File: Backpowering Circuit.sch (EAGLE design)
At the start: 4 parts, among them IC1 DMMT5401, Q1 DMP2305U-7

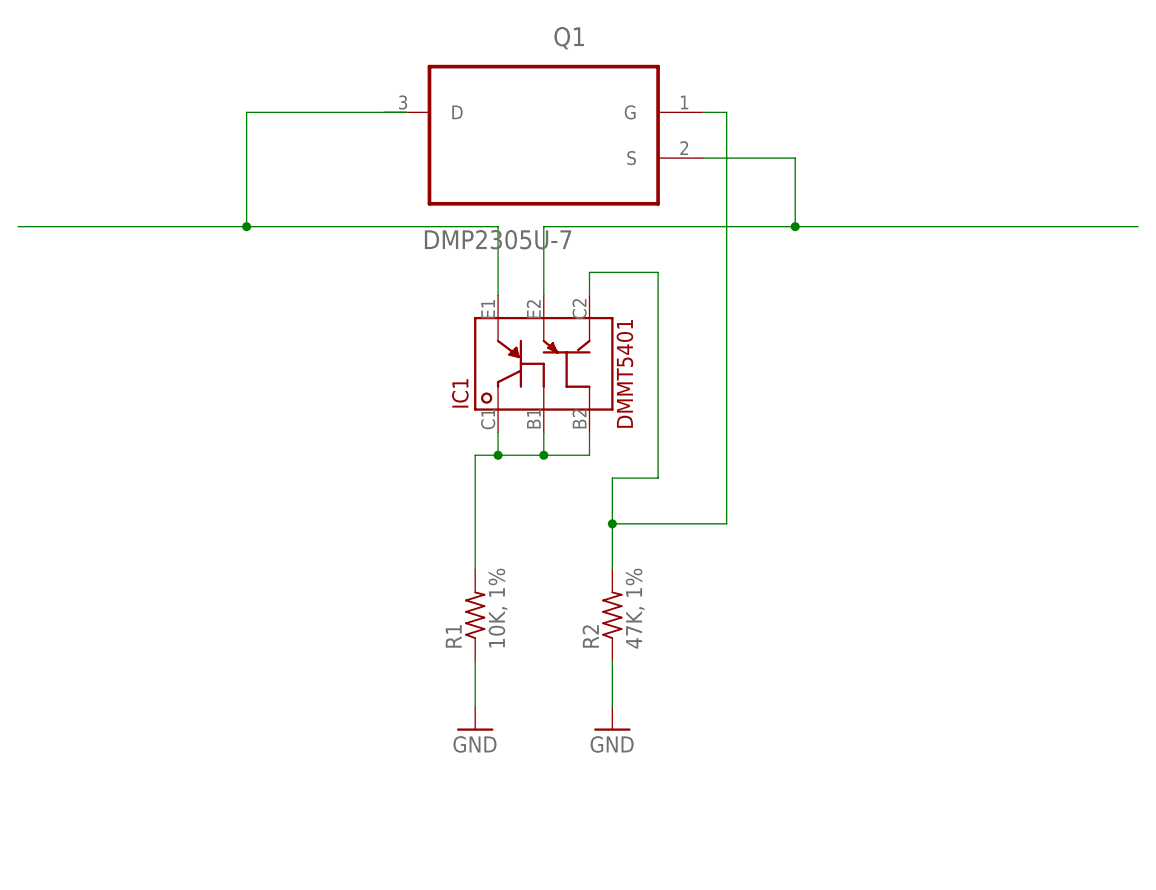
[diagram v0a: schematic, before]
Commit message: Convertd Backpowering Circuit schematic into a pluggable board.
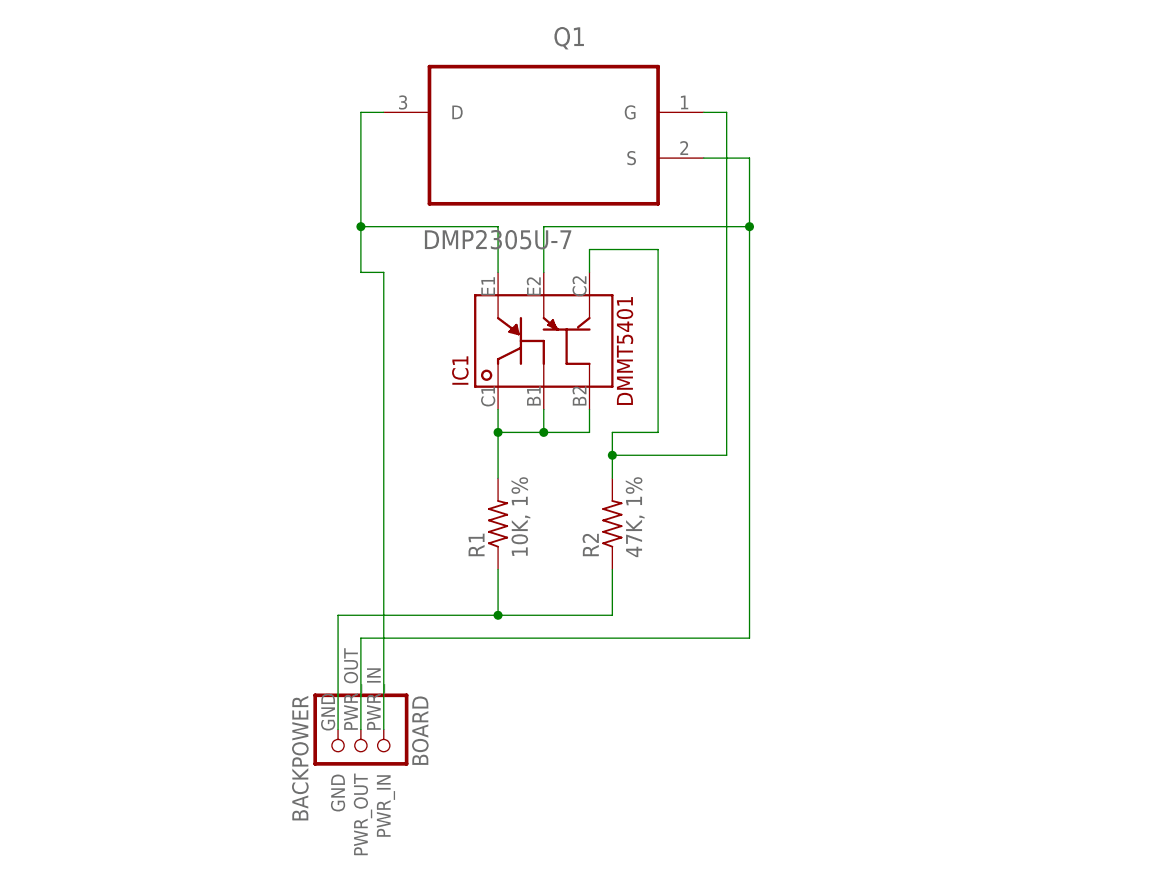
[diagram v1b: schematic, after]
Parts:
- added BOARD: BACKPOWER, connectors:BACKPOWER
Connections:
- removed net GND: R1.1, R2.1
- new net N$1: BOARD.GND, R1.1, R2.1
- net IN: now also BOARD.PWR_IN, Q1.D
- net OUT: now also BOARD.PWR_OUT
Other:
- moved on the sheet: IC1, R1, R2
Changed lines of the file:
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@@
 <part name="R1" library="adafruit" deviceset="R-US_" device="R1005" value="10K, 1%"/>
 <part name="R2" library="adafruit" deviceset="R-US_" device="R1005" value="47K, 1%"/>
-<part name="GND1" library="supply1" deviceset="GND" device=""/>
-<part name="GND2" library="supply1" deviceset="GND" device=""/>
+<part name="BOARD" library="connectors" deviceset="BACKPOWER" device=""/>
 </parts>
 <sheets>
@@
 <instances>
 <instance part="Q1" gate="A" x="27.94" y="71.12" rot="MR0"/>
-<instance part="IC1" gate="G$1" x="27.94" y="43.18"/>
-<instance part="R1" gate="G$1" x="20.32" y="15.24" rot="R90"/>
-<instance part="R2" gate="G$1" x="35.56" y="15.24" rot="R90"/>
-<instance part="GND1" gate="1" x="20.32" y="2.54"/>
-<instance part="GND2" gate="1" x="35.56" y="2.54"/>
+<instance part="IC1" gate="G$1" x="27.94" y="45.72"/>
+<instance part="R1" gate="G$1" x="22.86" y="25.4" rot="R90"/>
+<instance part="R2" gate="G$1" x="35.56" y="25.4" rot="R90"/>
+<instance part="BOARD" gate="G$1" x="7.62" y="0" rot="R270"/>
 </instances>
 <busses>
@@
 <net name="IN" class="0">
 <segment>
-<wire x1="-5.08" y1="58.42" x2="-30.48" y2="58.42" width="0.1524" layer="91"/>
-<wire x1="-5.08" y1="58.42" x2="-5.08" y2="71.12" width="0.1524" layer="91"/>
-<wire x1="-5.08" y1="71.12" x2="12.7" y2="71.12" width="0.1524" layer="91"/>
+<wire x1="7.62" y1="58.42" x2="7.62" y2="53.34" width="0.1524" layer="91"/>
+<wire x1="7.62" y1="58.42" x2="7.62" y2="71.12" width="0.1524" layer="91"/>
 <pinref part="IC1" gate="G$1" pin="E1"/>
-<wire x1="22.86" y1="50.8" x2="22.86" y2="58.42" width="0.1524" layer="91"/>
-<wire x1="22.86" y1="58.42" x2="-5.08" y2="58.42" width="0.1524" layer="91"/>
-<junction x="-5.08" y="58.42"/>
-</segment>
-</net>
-<net name="GND" class="0">
-<segment>
-<pinref part="GND1" gate="1" pin="GND"/>
-<pinref part="R1" gate="G$1" pin="1"/>
-<wire x1="20.32" y1="5.08" x2="20.32" y2="10.16" width="0.1524" layer="91"/>
-</segment>
-<segment>
-<pinref part="GND2" gate="1" pin="GND"/>
-<pinref part="R2" gate="G$1" pin="1"/>
-<wire x1="35.56" y1="5.08" x2="35.56" y2="10.16" width="0.1524" layer="91"/>
+<wire x1="22.86" y1="53.34" x2="22.86" y2="58.42" width="0.1524" layer="91"/>
+<wire x1="22.86" y1="58.42" x2="7.62" y2="58.42" width="0.1524" layer="91"/>
+<junction x="7.62" y="58.42"/>
+<pinref part="BOARD" gate="G$1" pin="PWR_IN"/>
+<wire x1="7.62" y1="53.34" x2="10.16" y2="53.34" width="0.1524" layer="91"/>
+<wire x1="10.16" y1="53.34" x2="10.16" y2="2.54" width="0.1524" layer="91"/>
+<pinref part="Q1" gate="A" pin="D"/>
+<wire x1="7.62" y1="71.12" x2="10.16" y2="71.12" width="0.1524" layer="91"/>
 </segment>
 </net>
 <net name="OUT" class="0">
 <segment>
-<wire x1="55.88" y1="58.42" x2="93.98" y2="58.42" width="0.1524" layer="91"/>
+<wire x1="50.8" y1="58.42" x2="50.8" y2="12.7" width="0.1524" layer="91"/>
 <pinref part="Q1" gate="A" pin="S"/>
-<wire x1="55.88" y1="58.42" x2="55.88" y2="66.04" width="0.1524" layer="91"/>
-<wire x1="55.88" y1="66.04" x2="45.72" y2="66.04" width="0.1524" layer="91"/>
+<wire x1="50.8" y1="58.42" x2="50.8" y2="66.04" width="0.1524" layer="91"/>
+<wire x1="50.8" y1="66.04" x2="45.72" y2="66.04" width="0.1524" layer="91"/>
 <pinref part="IC1" gate="G$1" pin="E2"/>
-<wire x1="27.94" y1="50.8" x2="27.94" y2="58.42" width="0.1524" layer="91"/>
-<wire x1="27.94" y1="58.42" x2="55.88" y2="58.42" width="0.1524" layer="91"/>
-<junction x="55.88" y="58.42"/>
+<wire x1="27.94" y1="53.34" x2="27.94" y2="58.42" width="0.1524" layer="91"/>
+<wire x1="27.94" y1="58.42" x2="50.8" y2="58.42" width="0.1524" layer="91"/>
+<junction x="50.8" y="58.42"/>
+<wire x1="50.8" y1="12.7" x2="7.62" y2="12.7" width="0.1524" layer="91"/>
+<pinref part="BOARD" gate="G$1" pin="PWR_OUT"/>
+<wire x1="7.62" y1="12.7" x2="7.62" y2="2.54" width="0.1524" layer="91"/>
 </segment>
 </net>
@@
 <segment>
 <pinref part="IC1" gate="G$1" pin="C1"/>
-<wire x1="22.86" y1="35.56" x2="22.86" y2="33.02" width="0.1524" layer="91"/>
-<wire x1="22.86" y1="33.02" x2="20.32" y2="33.02" width="0.1524" layer="91"/>
+<wire x1="22.86" y1="38.1" x2="22.86" y2="35.56" width="0.1524" layer="91"/>
 <pinref part="R1" gate="G$1" pin="2"/>
-<wire x1="20.32" y1="33.02" x2="20.32" y2="20.32" width="0.1524" layer="91"/>
+<wire x1="22.86" y1="35.56" x2="22.86" y2="30.48" width="0.1524" layer="91"/>
 <pinref part="IC1" gate="G$1" pin="B1"/>
-<wire x1="27.94" y1="35.56" x2="27.94" y2="33.02" width="0.1524" layer="91"/>
-<wire x1="27.94" y1="33.02" x2="22.86" y2="33.02" width="0.1524" layer="91"/>
-<junction x="22.86" y="33.02"/>
+<wire x1="27.94" y1="38.1" x2="27.94" y2="35.56" width="0.1524" layer="91"/>
+<wire x1="27.94" y1="35.56" x2="22.86" y2="35.56" width="0.1524" layer="91"/>
+<junction x="22.86" y="35.56"/>
 <pinref part="IC1" gate="G$1" pin="B2"/>
-<wire x1="33.02" y1="35.56" x2="33.02" y2="33.02" width="0.1524" layer="91"/>
-<wire x1="33.02" y1="33.02" x2="27.94" y2="33.02" width="0.1524" layer="91"/>
-<junction x="27.94" y="33.02"/>
+<wire x1="33.02" y1="38.1" x2="33.02" y2="35.56" width="0.1524" layer="91"/>
+<wire x1="33.02" y1="35.56" x2="27.94" y2="35.56" width="0.1524" layer="91"/>
+<junction x="27.94" y="35.56"/>
 </segment>
 </net>
@@
 <segment>
 <pinref part="IC1" gate="G$1" pin="C2"/>
-<wire x1="33.02" y1="50.8" x2="33.02" y2="53.34" width="0.1524" layer="91"/>
-<wire x1="33.02" y1="53.34" x2="40.64" y2="53.34" width="0.1524" layer="91"/>
-<wire x1="40.64" y1="53.34" x2="40.64" y2="30.48" width="0.1524" layer="91"/>
-<wire x1="40.64" y1="30.48" x2="35.56" y2="30.48" width="0.1524" layer="91"/>
+<wire x1="33.02" y1="53.34" x2="33.02" y2="55.88" width="0.1524" layer="91"/>
+<wire x1="33.02" y1="55.88" x2="40.64" y2="55.88" width="0.1524" layer="91"/>
+<wire x1="40.64" y1="55.88" x2="40.64" y2="35.56" width="0.1524" layer="91"/>
+<wire x1="40.64" y1="35.56" x2="35.56" y2="35.56" width="0.1524" layer="91"/>
 <pinref part="R2" gate="G$1" pin="2"/>
-<wire x1="35.56" y1="30.48" x2="35.56" y2="25.4" width="0.1524" layer="91"/>
+<wire x1="35.56" y1="35.56" x2="35.56" y2="33.02" width="0.1524" layer="91"/>
 <pinref part="Q1" gate="A" pin="G"/>
-<wire x1="35.56" y1="25.4" x2="35.56" y2="20.32" width="0.1524" layer="91"/>
+<wire x1="35.56" y1="33.02" x2="35.56" y2="30.48" width="0.1524" layer="91"/>
 <wire x1="45.72" y1="71.12" x2="48.26" y2="71.12" width="0.1524" layer="91"/>
-<wire x1="48.26" y1="71.12" x2="48.26" y2="25.4" width="0.1524" layer="91"/>
-<wire x1="35.56" y1="25.4" x2="48.26" y2="25.4" width="0.1524" layer="91"/>
-<junction x="35.56" y="25.4"/>
+<wire x1="48.26" y1="71.12" x2="48.26" y2="33.02" width="0.1524" layer="91"/>
+<wire x1="35.56" y1="33.02" x2="48.26" y2="33.02" width="0.1524" layer="91"/>
+<junction x="35.56" y="33.02"/>
 </segment>
 </net>
+<net name="N$1" class="0">
+<segment>
+<pinref part="R1" gate="G$1" pin="1"/>
+<wire x1="22.86" y1="15.24" x2="22.86" y2="20.32" width="0.1524" layer="91"/>
+<pinref part="R2" gate="G$1" pin="1"/>
+<wire x1="35.56" y1="15.24" x2="35.56" y2="20.32" width="0.1524" layer="91"/>
+<wire x1="22.86" y1="15.24" x2="35.56" y2="15.24" width="0.1524" layer="91"/>
+<wire x1="22.86" y1="15.24" x2="5.08" y2="15.24" width="0.1524" layer="91"/>
+<junction x="22.86" y="15.24"/>
+<pinref part="BOARD" gate="G$1" pin="GND"/>
+<wire x1="5.08" y1="15.24" x2="5.08" y2="2.54" width="0.1524" layer="91"/>
+</segment>
+</net>
